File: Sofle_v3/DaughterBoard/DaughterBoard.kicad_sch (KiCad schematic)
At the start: 2 parts, among them SW1 RotaryEncoder_Switch, SW2 RotaryEncoder_Switch

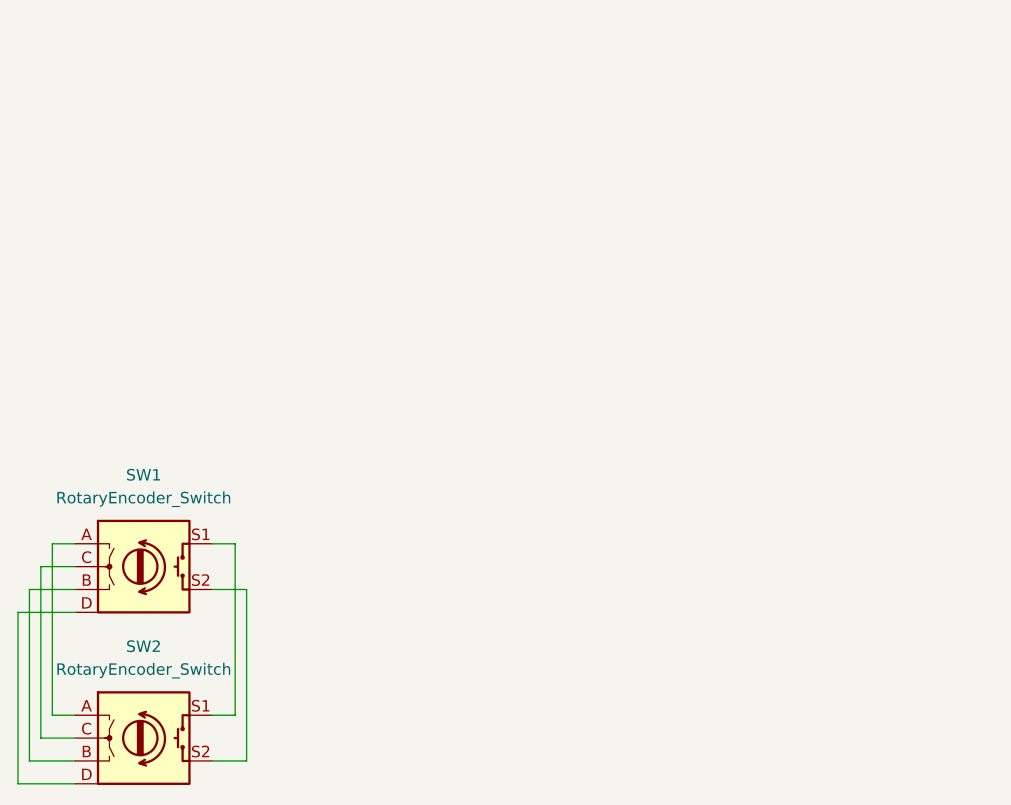
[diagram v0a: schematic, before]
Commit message: Design: Fixed daughterboard pinout/Made it configurable
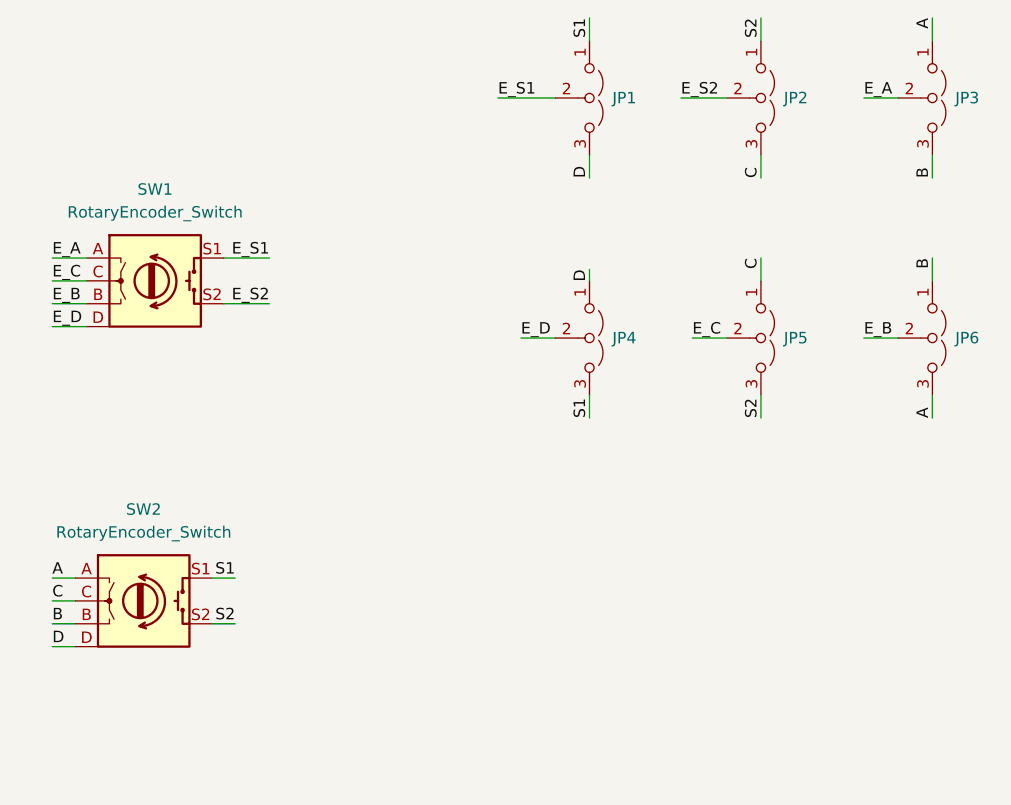
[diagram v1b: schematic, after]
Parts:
- added JP1, JP2, JP3, JP4, JP5, JP6: Jumper_3_Open, Jumper:SolderJumper-3_P1.3mm_Open_Pad1.0x1.5mm, symbol Jumper:Jumper_3_Open
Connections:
- net A: now reaches SW2.A
- net A: now also JP3.1 (A), JP6.3 (B); no longer SW1.A
- net B: now reaches SW2.B
- net B: now also JP3.3 (B), JP6.1 (A); no longer SW1.B
- net C: now reaches SW2.C
- net C: now also JP2.3 (B), JP5.1 (A); no longer SW1.C
- net D: now reaches SW2.D
- net D: now also JP1.3 (B), JP4.1 (A); no longer SW1.D
- net E_S1: now reaches SW1.S1
- net E_S1: now also JP1.2 (C); no longer SW2.S1
- net E_S2: now reaches SW1.S2
- net E_S2: now also JP2.2 (C); no longer SW2.S2
- new net E_A: JP3.2 (C), SW1.A
- new net E_B: JP6.2 (C), SW1.B
- new net E_C: JP5.2 (C), SW1.C
- new net E_D: JP4.2 (C), SW1.D
- new net S1: JP1.1 (A), JP4.3 (B), SW2.S1
- new net S2: JP2.1 (A), JP5.3 (B), SW2.S2
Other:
- moved on the sheet: SW1, SW2
